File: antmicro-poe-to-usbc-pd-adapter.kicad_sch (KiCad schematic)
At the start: 102 parts, among them J1 Bus_RJ45_5-2337992-8, J2 Bus_RJ45_5-2337992-8, J3 USB-C_GCT_USB4105-GF-A, Q1 PJE138K, U1 TPS2372-3RGWR, U2 LV14540DDAR, U3 INA230AIRGTR, U4 IEA48003A280V-001-R, U5 FT4232H_VQFN, U6 TPS65987DDHRSHR, U7 LV14540DDAR, U8 W25Q80DV_SOIC-8, U9 74CBTLV3257_VQFN, Y1 Resonator_12MHz_ABM8G

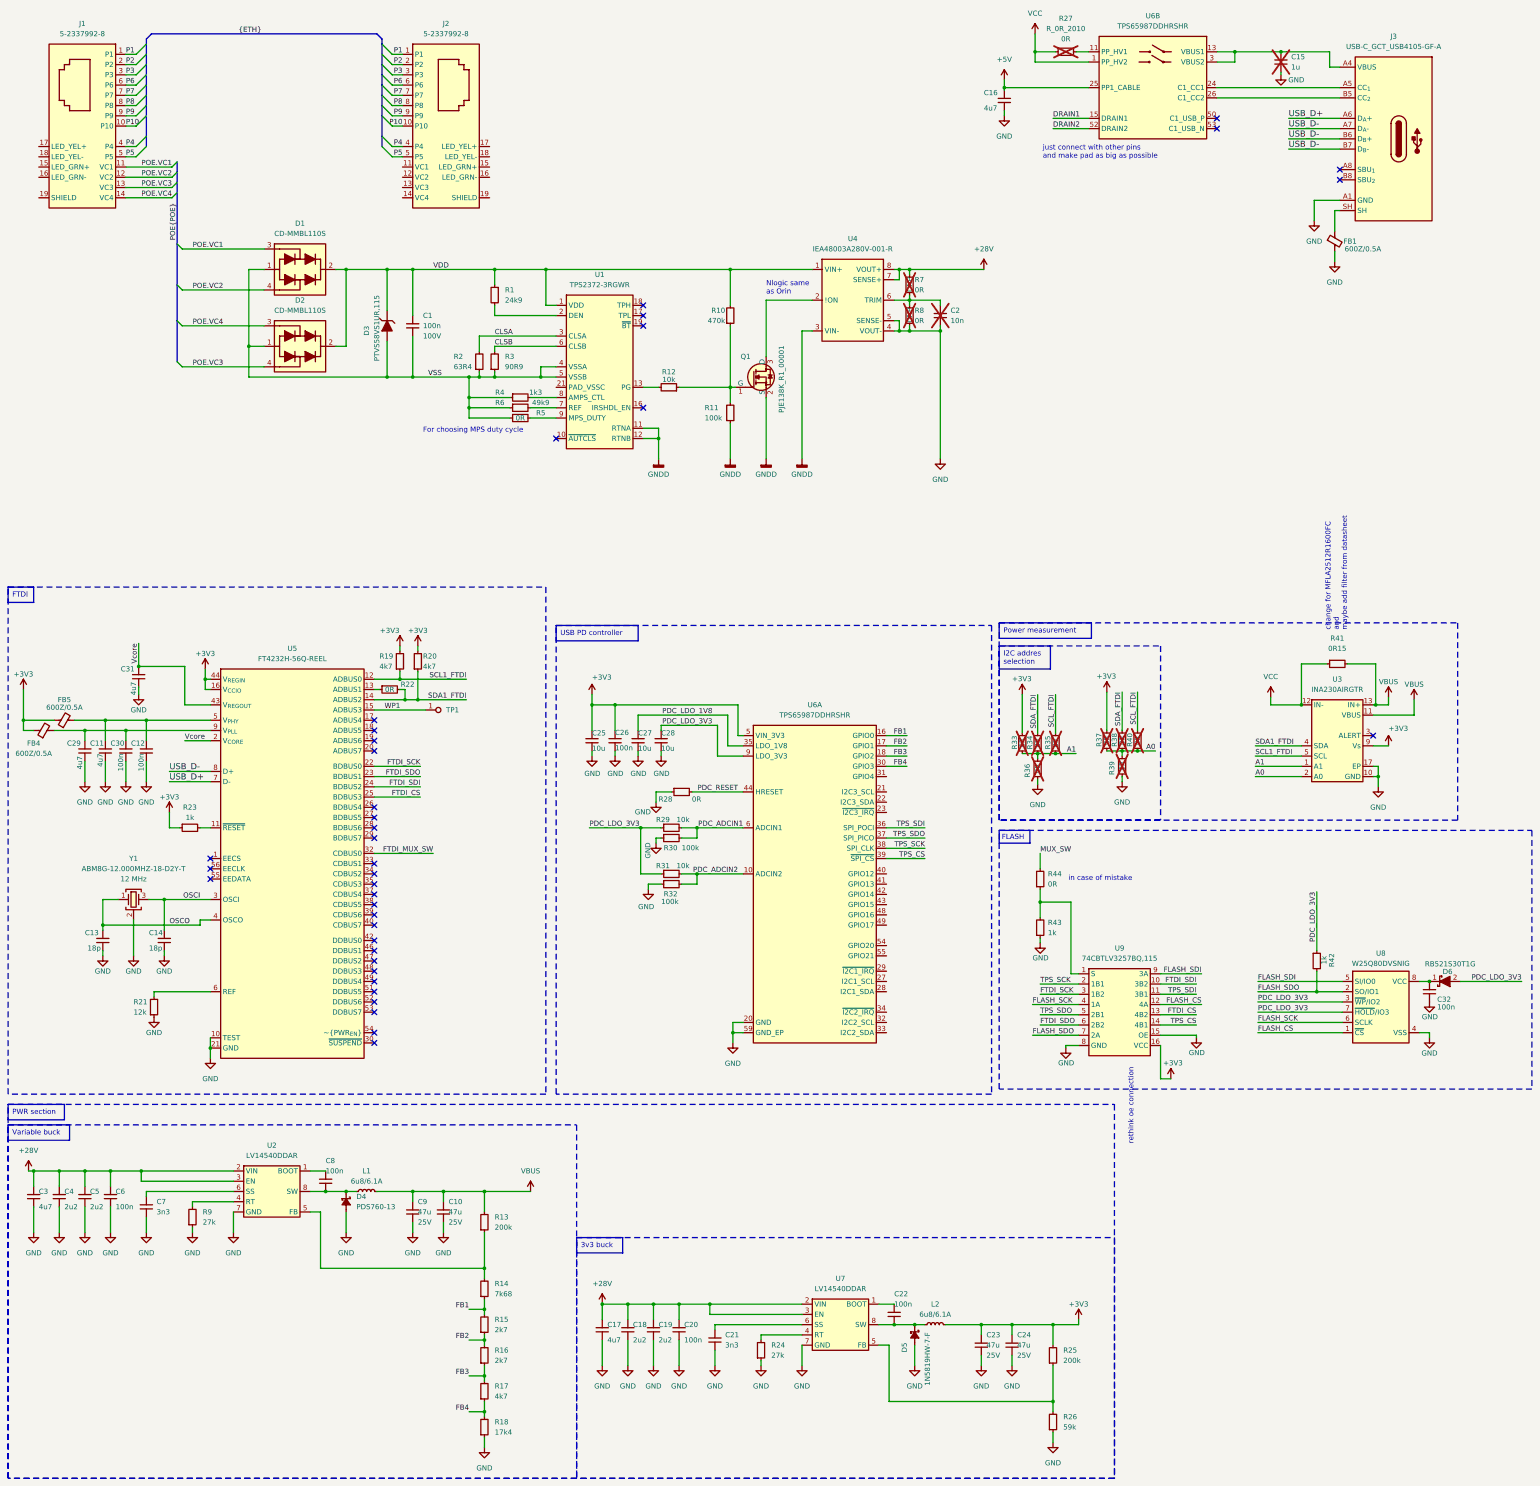
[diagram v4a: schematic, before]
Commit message: [#62623] Improved schematic, added hierarchy
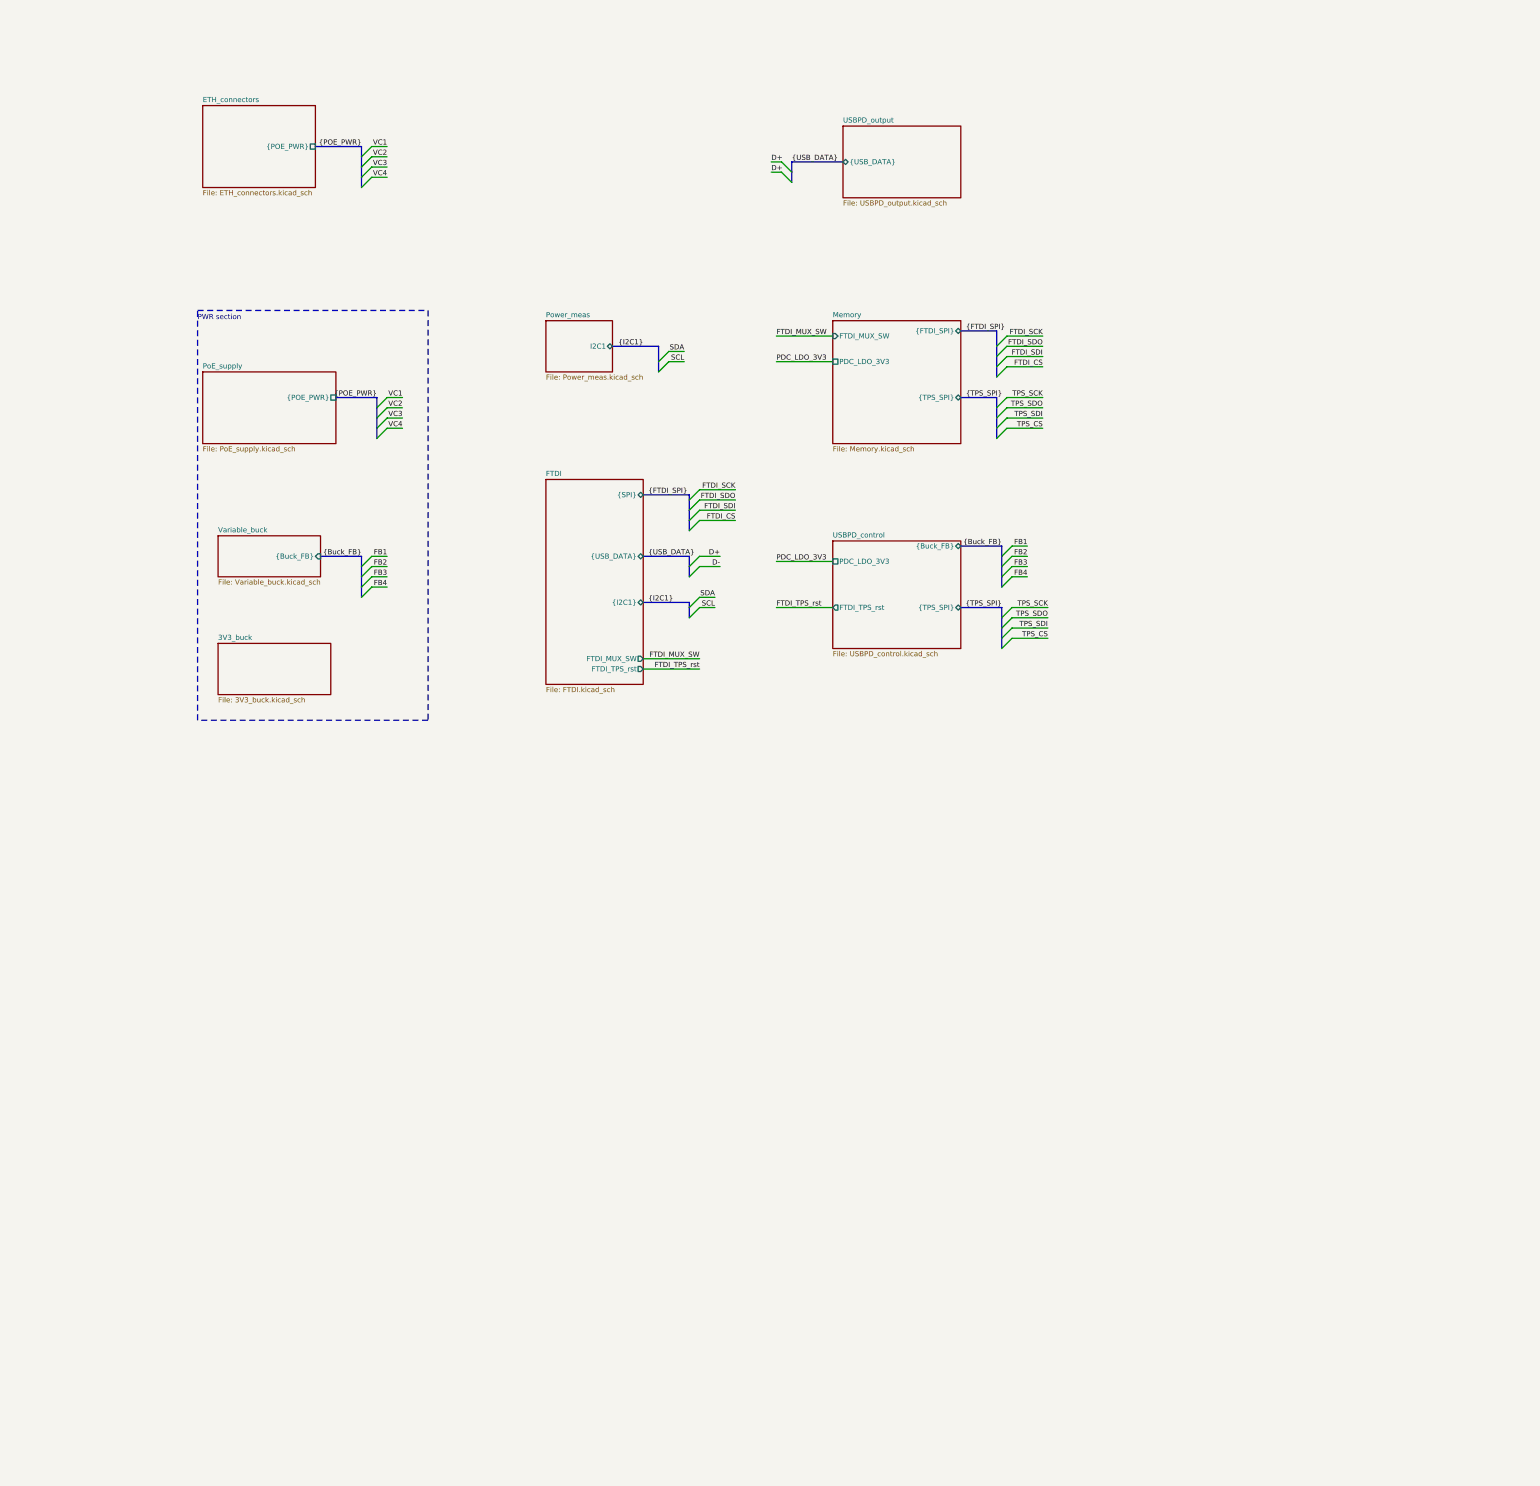
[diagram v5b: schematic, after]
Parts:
- removed C1: C_100n_100V_0805, antmicro-footprints:C_0805_2012Metric, symbol antmicroCapacitorsmisc:C_100n_100V_0805
- removed C10, C23, C24, C9: C_47u_25V_1206, antmicro-footprints:C_1206_3216Metric, symbol antmicroCapacitorsmisc:C_47u_25V_1206
- removed C11, C16, C29, C31: C_4u7_25V_0402, antmicro-footprints:C_0402_1005Metric, symbol antmicroCapacitors0402:C_4u7_25V_0402
- removed C12, C30: C_100n_16V_X7R_0402, antmicro-footprints:C_0402_1005Metric, symbol antmicroCapacitors0402:C_100n_16V_X7R_0402
- removed C13, C14: C_18p_0402, antmicro-footprints:C_0402_1005Metric, symbol antmicroCapacitors0402:C_18p_0402
- removed C15: C_1u_25V_0402, antmicro-footprints:C_0402_1005Metric, symbol antmicroCapacitors0402:C_1u_25V_0402
- removed C17, C3: C_4u7_1210_100V, antmicro-footprints:C_1210_3225Metric, symbol antmicroCapacitorsmisc:C_4u7_1210_100V
- removed C18, C19, C4, C5: C_2u2_1210, antmicro-footprints:C_1210_3225Metric, symbol antmicroCapacitorsmisc:C_2u2_1210
- removed C2: C_10n_50V_X7R_0402, antmicro-footprints:C_0402_1005Metric, symbol antmicroCapacitors0402:C_10n_50V_X7R_0402
- removed C20, C22, C6, C8: C_100n_100V_X7R_0603, antmicro-footprints:C_0603_1608Metric, symbol antmicroCapacitors0603:C_100n_100V_X7R_0603
- removed C21, C7: C_3n3_0402, antmicro-footprints:C_0402_1005Metric, symbol antmicroCapacitors0402:C_3n3_0402
- removed C25, C27, C28: C_10u_0402, antmicro-footprints:C_0402_1005Metric, symbol antmicroCapacitors0402:C_10u_0402
- removed C26, C32: C_100n_0402, antmicro-footprints:C_0402_1005Metric, symbol antmicroCapacitors0402:C_100n_0402
- removed D1, D2: CD-MMBL110S, antmicro-footprints:DFN3538, symbol antmicroDiodesRectifiersSingle:CD-MMBL110S
- removed D3: PTVS58VS1UR,115, antmicro-footprints:D_SOD-123F, symbol antmicroTVSDiodes:PTVS58VS1UR,115
- removed D4: PDS760, antmicro-footprints:PowerDI5, symbol antmicroDiodesRectifiersSingle:PDS760
- removed D5: 1N5819HW-7-F, antmicro-footprints:D_SOD-123, symbol antmicroDiodesRectifiersSingle:1N5819HW-7-F
- removed D6: RB521S30T1G, antmicro-footprints:SOD-523, symbol antmicroDiodesRectifiersSingle:RB521S30T1G
- removed FB1, FB4, FB5: FB_600Z_0.5A_Murata-BLM18AG_0603, antmicro-footprints:FB_0603_1608Metric, symbol antmicroFerriteBeadsandChips:FB_600Z_0.5A_Murata-BLM18AG_0603
- removed J1, J2: Bus_RJ45_5-2337992-8, antmicro-footprints:RJ45_X-2337992-8_Horizontal, symbol antmicroModularConnectorsJacksWithMagnetics:Bus_RJ45_5-2337992-8
- removed J3: USB-C_GCT_USB4105-GF-A, antmicro-footprints:USB-C_Receptacle_GCT_USB4105-GF-A, symbol antmicroUSBConnectors:USB-C_GCT_USB4105-GF-A
- removed L1, L2: L_6u8_6.1A_MPS-MPL-AL5050, antmicro-footprints:L_MPS-MPL-AL5050, symbol antmicroFixedInductors:L_6u8_6.1A_MPS-MPL-AL5050
- removed Q1: PJE138K, antmicro-footprints:SOT-523, symbol antmicroTransistorsFETsMOSFETsSingle:PJE138K
- removed R1: R_24k9_0402, antmicro-footprints:R_0402_1005Metric, symbol antmicroResistors0402:R_24k9_0402
- removed R10: R_470k_0402, antmicro-footprints:R_0402_1005Metric, symbol antmicroResistors0402:R_470k_0402
- removed R11, R30, R32: R_100k_0402, antmicro-footprints:R_0402_1005Metric, symbol antmicroResistors0402:R_100k_0402
- removed R12, R29, R31: R_10k_0402, antmicro-footprints:R_0402_1005Metric, symbol antmicroResistors0402:R_10k_0402
- removed R13, R25: R_200k_0402, antmicro-footprints:R_0402_1005Metric, symbol antmicroResistors0402:R_200k_0402
- removed R14: R_7k68_0402, antmicro-footprints:R_0402_1005Metric, symbol antmicroResistors0402:R_7k68_0402
- removed R15, R16: R_2k7_0402, antmicro-footprints:R_0402_1005Metric, symbol antmicroResistors0402:R_2k7_0402
- removed R17, R19, R20: R_4k7_0402, antmicro-footprints:R_0402_1005Metric, symbol antmicroResistors0402:R_4k7_0402
- removed R18: R_17k4_0402, antmicro-footprints:R_0402_1005Metric, symbol antmicroResistors0402:R_17k4_0402
- removed R2: R_63R4_0603, antmicro-footprints:R_0603_1608Metric, symbol antmicroResistors0603:R_63R4_0603
- removed R21: R_12k_0402, antmicro-footprints:R_0402_1005Metric, symbol antmicroResistors0402:R_12k_0402
- removed R22, R28, R33, R34, R35, R36, R37, R38, R39, R40, R44, R5: R_0R_0402, antmicro-footprints:R_0402_1005Metric, symbol antmicroResistors0402:R_0R_0402
- removed R23, R42, R43: R_1k_0402, antmicro-footprints:R_0402_1005Metric, symbol antmicroResistors0402:R_1k_0402
- removed R24, R9: R_27k_0402, antmicro-footprints:R_0402_1005Metric, symbol antmicroResistors0402:R_27k_0402
- removed R26: R_59k_0402, antmicro-footprints:R_0402_1005Metric, symbol antmicroResistors0402:R_59k_0402
- removed R27: R_0R_2010, antmicro-footprints:R_2010_5025Metric, symbol antmicroResistorsmisc:R_0R_2010
- removed R3: R_90R9_0603, antmicro-footprints:R_0603_1608Metric, symbol antmicroResistors0603:R_90R9_0603
- removed R4: R_1k3_0402, antmicro-footprints:R_0402_1005Metric, symbol antmicroResistors0402:R_1k3_0402
- removed R41: R_0R15_2010, antmicro-footprints:R_2010_5025Metric, symbol antmicroResistorsmisc:R_0R15_2010
- removed R6: R_49k9_0402, antmicro-footprints:R_0402_1005Metric, symbol antmicroResistors0402:R_49k9_0402
- removed R7, R8: R_0R_0603, antmicro-footprints:R_0603_1608Metric, symbol antmicroResistors0603:R_0R_0603
- removed TP1: TP_1.5mm_SMD, antmicro-footprints:TP_SMD_1.5mm, symbol antmicroTestPoints:TP_1.5mm_SMD
- removed U1: TPS2372-3RGWR, antmicro-footprints:VQFN-20_5x5x1mm_P0.65mm, symbol antmicroPMICPowerDistributionSwitchesLoadDrivers:TPS2372-3RGWR
- removed U2, U7: LV14540DDAR, antmicro-footprints:SOIC-8-1EP_3.9x4.9x1.75mm_P1.27mm_EP_vias, symbol antmicroDCDCConverters:LV14540DDAR
- removed U3: INA230AIRGTR, antmicro-footprints:VQFN-16-1EP_3x3mm_P0.5mm_EP1.68x1.68mm, symbol antmicroPowerMeasurement:INA230AIRGTR
- removed U4: IEA48003A280V-001-R, antmicro-footprints:IEA48003A280V-001-R, symbol antmicroDCDCConverters:IEA48003A280V-001-R
- removed U5: FT4232H_VQFN, antmicro-footprints:QFN-56-1EP_8x8mm_P0.5mm, symbol antmicroInterfaceControllers:FT4232H_VQFN
- removed U6: TPS65987DDHRSHR, antmicro-footprints:IC_TPS65987DDHRSHR, symbol antmicroInterfaceControllers:TPS65987DDHRSHR
- removed U8: W25Q80DV_SOIC-8, antmicro-footprints:SOIC-8_3.9x4.9x1.75mm_P1.27mm, symbol antmicroMemory:W25Q80DV_SOIC-8
- removed U9: 74CBTLV3257_VQFN, antmicro-footprints:DHVQFN-16-1EP_2.5x3.5mm_P0.5mm, symbol antmicroInterfaceAnalogSwitchesMultiplexersDemultiplexers:74CBTLV3257_VQFN
- removed Y1: Resonator_12MHz_ABM8G, antmicro-footprints:Resonator_SMD_Abracon_ABM8G_3.2x2.5mm, symbol antmicroResonators:Resonator_12MHz_ABM8G
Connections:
- no-connect marks 38 -> 0
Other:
- added sheet 3V3_buck (3V3_buck.kicad_sch)
- added sheet ETH_connectors (ETH_connectors.kicad_sch)
- added sheet FTDI (FTDI.kicad_sch)
- added sheet Memory (Memory.kicad_sch)
- added sheet PoE_supply (PoE_supply.kicad_sch)
- added sheet Power_meas (Power_meas.kicad_sch)
- added sheet USBPD_control (USBPD_control.kicad_sch)
- added sheet USBPD_output (USBPD_output.kicad_sch)
- added sheet Variable_buck (Variable_buck.kicad_sch)
- note added: "PWR section"
- note removed: "FLASH"
- note removed: "For choosing MPS duty cycle"
- note removed: "Nlogic same as Orin"
- note removed: "change for MFLA2512R1600FC and maybe add filter from datasheet"
- note removed: "in case of mistake"
- note removed: "just connect with other pins and make pad as big as possible"
- note removed: "rethink oe connection"
